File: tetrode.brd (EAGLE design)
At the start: 108 x 101.6 mm, 34 parts, among them IC1 MEGA8-P, J1 AVR_SPI_PROG_3X2NS, U1 LM2576T-5.0/NOPB, Y1 16MHz

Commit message: Started code
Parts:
- removed C5: 22p, resistor:C025-024X044
- removed C6: 470u, resistor:E5-13
- removed C7: 47u, resistor:E2,5-6
- removed D2: (no value), adafruit:DO-1N4148
- removed D3: (no value), adafruit:DO201T15
- removed L1: 100u, resistor:0204/5
- removed P1, P2, P3: (no value), SparkFun-Connectors:1X03
- removed U1: LM2576T-5.0/NOPB, LM2576T:T05A_TEX
- added J2, J3, J4: (no value), SparkFun-Connectors:1X05
- C1: value 47u -> 2.2u; device resistor:E2,5-6 -> resistor:E2-5
- C2: value 470u -> 2.2u; device resistor:E5-13 -> resistor:E2-5
- C4: value 22p -> 2.2u; device resistor:C025-024X044 -> resistor:E2-5
- Y1: value 16MHz -> (none); device SparkFun-Clocks:HC49US -> SparkFun-Clocks:RESONATOR-PTH-7.6X3.8
- moved C4 81.3 mm to (3.81, 49.5)
- moved J1 80.1 mm to (76.2, 5.08)
- moved S2 78.5 mm to (21.6, 69.8)
- moved R5 70.7 mm to (21.6, 61.7)
- moved S3 68.8 mm to (38.1, 69.8)
- moved S4 64.9 mm to (55.9, 69.8)
- moved R6 53.6 mm to (38.1, 61.8)
- moved R4 50.4 mm to (50.8, 47.6)
- moved C2 49.0 mm to (64.8, 50.8)
- moved R8 44.9 mm to (59.7, 50.8), turned to 90 degrees
- moved R2 44.7 mm to (6.35, 62.2), turned to 90 degrees
- moved R7 35.6 mm to (55.9, 61.8)
- moved C1 30.0 mm to (7.62, 69.8)
- moved C3 25.0 mm to (64.8, 57.1)
- moved LS1 16.6 mm to (71.1, 66.0)
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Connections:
- removed net N$5: IC1.25, P3.2
- removed net N$8: D3.C, L1.2, U1.2
- removed net VCC: C1.+, C7.+, D2.C, U1.1
- net +5V: now also CN1.PWR, J2.1, J3.1, J4.1; no longer C2.+, C6.+, L1.1, P1.1, P2.1, P3.1, U1.4
- net GND: now also C4.-, J2.5, J3.5, J4.5, Y1.2; no longer C4.2, C5.2, C6.-, C7.-, D3.A, P1.3, P2.3, P3.3, U1.3, U1.5
- net N$1: now also IC1.23, J2.3; no longer CN1.PWR, D2.A
- net N$3: now also IC1.24, J3.3; no longer IC1.23, P1.2
- net N$4: now also IC1.25, J4.3; no longer IC1.24, P2.2
- net SW1: now also C1.+
- net SW2: now also C2.+
- net SW3: now also C4.+
- net XTAL1: no longer C4.1
- net XTAL2: now also Y1.3; no longer C5.1, Y1.2
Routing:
- net SW3: track 0.00 -> 116.9 mm, vias 0 -> 2
- net RST: track 0.00 -> 107.5 mm
- net RS: track 0.00 -> 96.4 mm, vias 0 -> 1
- net E: track 0.00 -> 93.7 mm, vias 0 -> 1
- net SCK: track 0.00 -> 81.4 mm
- net SW2: track 0.00 -> 81.4 mm
- net VO: track 0.00 -> 81.0 mm, vias 0 -> 1
- net N$4: track 0.00 -> 70.9 mm, vias 0 -> 3
- net XTAL1: track 0.00 -> 64.2 mm, vias 0 -> 2
- net N$3: track 0.00 -> 61.5 mm, vias 0 -> 3
- net N$1: track 0.00 -> 61.4 mm
- net N$7: track 0.00 -> 61.1 mm
- net XTAL2: track 0.00 -> 59.3 mm, vias 0 -> 3
- net SW1: track 0.00 -> 51.4 mm
- net S_FEED: track 0.00 -> 43.7 mm, vias 0 -> 1
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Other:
- board size 108 x 101.6 mm -> 81.3 x 85.1 mm

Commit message: Updates to CAD for board and base, started on code
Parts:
- moved S1 12.7 mm to (29.2, 82.5)
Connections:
- net +5V: now also S1.2; no longer S1.1
- net GND: now also S1.1; no longer S1.2
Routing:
- net S_FEED: track 43.7 -> 56.4 mm
- net SERVO: track 40.0 -> 46.1 mm
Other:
- board text added: "FEEDBACK"
- board text added: "SERVO"
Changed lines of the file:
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@@
 <hole x="49.53" y="5.08" drill="3.401059375"/>
 <hole x="11.43" y="62.23" drill="3.401059375"/>
+<text x="39.37" y="81.28" size="1.778" layer="21">FEEDBACK</text>
+<text x="28.829" y="79.756" size="1.27" layer="21">SERVO</text>
 </plain>
 <attributes>
@@
 <attribute name="VALUE" x="35.9664" y="59.5376" size="0.9906" layer="27" ratio="10"/>
 </element>
-<element name="S1" library="SparkFun-Connectors" library_urn="urn:adsk.eagle:library:513" package="1X04" package3d_urn="urn:adsk.eagle:package:38085/1" value="" x="16.51" y="82.55" smashed="yes">
-<attribute name="NAME" x="15.24" y="83.947" size="0.6096" layer="25" font="vector" ratio="20"/>
-<attribute name="PROD_ID" value="CONN-09696" x="90.17" y="7.62" size="1.778" layer="27" display="off"/>
-<attribute name="VALUE" x="15.24" y="80.518" size="0.6096" layer="27" font="vector" ratio="20"/>
+<element name="S1" library="SparkFun-Connectors" library_urn="urn:adsk.eagle:library:513" package="1X04" package3d_urn="urn:adsk.eagle:package:38085/1" value="" x="29.21" y="82.55" smashed="yes">
+<attribute name="NAME" x="27.94" y="83.947" size="0.6096" layer="25" font="vector" ratio="20"/>
+<attribute name="PROD_ID" value="CONN-09696" x="102.87" y="7.62" size="1.778" layer="27" display="off"/>
+<attribute name="VALUE" x="27.94" y="80.518" size="0.6096" layer="27" font="vector" ratio="20"/>
 </element>
 <element name="VR1" library="SparkFun-Resistors" library_urn="urn:adsk.eagle:library:532" package="TRIMPOT-PTH-3386U" package3d_urn="urn:adsk.eagle:package:39662/1" value="10k" x="74.93" y="52.07" smashed="yes">
@@
 <contactref element="R1" pad="2"/>
 <contactref element="R3" pad="2"/>
-<contactref element="S1" pad="1"/>
 <contactref element="LCD1" pad="2"/>
 <contactref element="R4" pad="2"/>
@@
 <contactref element="J3" pad="1"/>
 <contactref element="J4" pad="1"/>
+<contactref element="S1" pad="2"/>
 </signal>
 <signal name="RST">
@@
 <contactref element="CN1" pad="GNDBREAK"/>
 <contactref element="D1" pad="K"/>
-<contactref element="S1" pad="2"/>
 <contactref element="LCD1" pad="16"/>
 <contactref element="LCD1" pad="1"/>
@@
 <wire x1="18.8" y1="43.44" x2="16.52" y2="45.72" width="0.254" layer="1"/>
 <wire x1="16.52" y1="45.72" x2="11.43" y2="45.72" width="0.254" layer="1"/>
+<contactref element="S1" pad="1"/>
 </signal>
 <signal name="N$2">
@@
 <wire x1="14.27353125" y1="65.87216875" x2="13.2715" y2="66.8742" width="0.254" layer="16"/>
 <wire x1="13.2715" y1="66.8742" x2="13.2715" y2="74.2315" width="0.254" layer="16"/>
-<wire x1="23.3142125" y1="82.55" x2="24.13" y2="82.55" width="0.254" layer="16"/>
-<wire x1="20.3708" y1="81.3308" x2="22.0950125" y2="81.3308" width="0.254" layer="16"/>
-<wire x1="22.0950125" y1="81.3308" x2="23.3142125" y2="82.55" width="0.254" layer="16"/>
+<wire x1="35.6108" y1="81.3308" x2="36.83" y2="82.55" width="0.254" layer="16"/>
+<wire x1="35.6108" y1="81.3308" x2="20.3708" y2="81.3308" width="0.254" layer="16"/>
 <wire x1="13.2715" y1="74.2315" x2="20.3708" y2="81.3308" width="0.254" layer="16"/>
 </signal>
@@
 <wire x1="24.13" y1="66.04" x2="24.13" y2="77.47" width="0.254" layer="16"/>
 <via x="24.13" y="77.47" extent="1-16" drill="0.35"/>
-<wire x1="24.13" y1="77.47" x2="24.13" y2="80.01" width="0.254" layer="1"/>
-<wire x1="24.13" y1="80.01" x2="21.59" y2="82.55" width="0.254" layer="1"/>
+<wire x1="34.29" y1="82.55" x2="29.21" y2="77.47" width="0.254" layer="1"/>
+<wire x1="24.13" y1="77.47" x2="29.21" y2="77.47" width="0.254" layer="1"/>
 </signal>
 <signal name="RS">

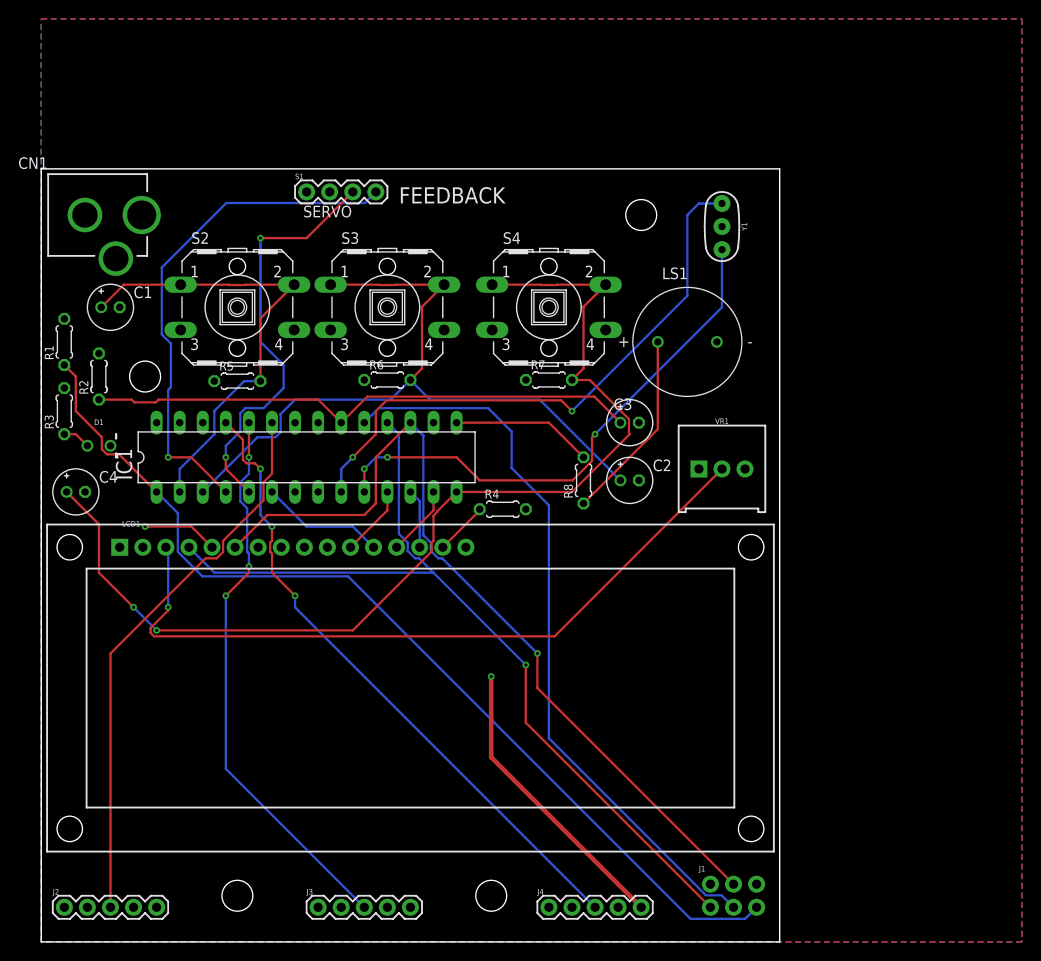
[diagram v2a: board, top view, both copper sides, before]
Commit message: Switched layout of board and reduced max speed of servo to resolve brown out when the servo stops
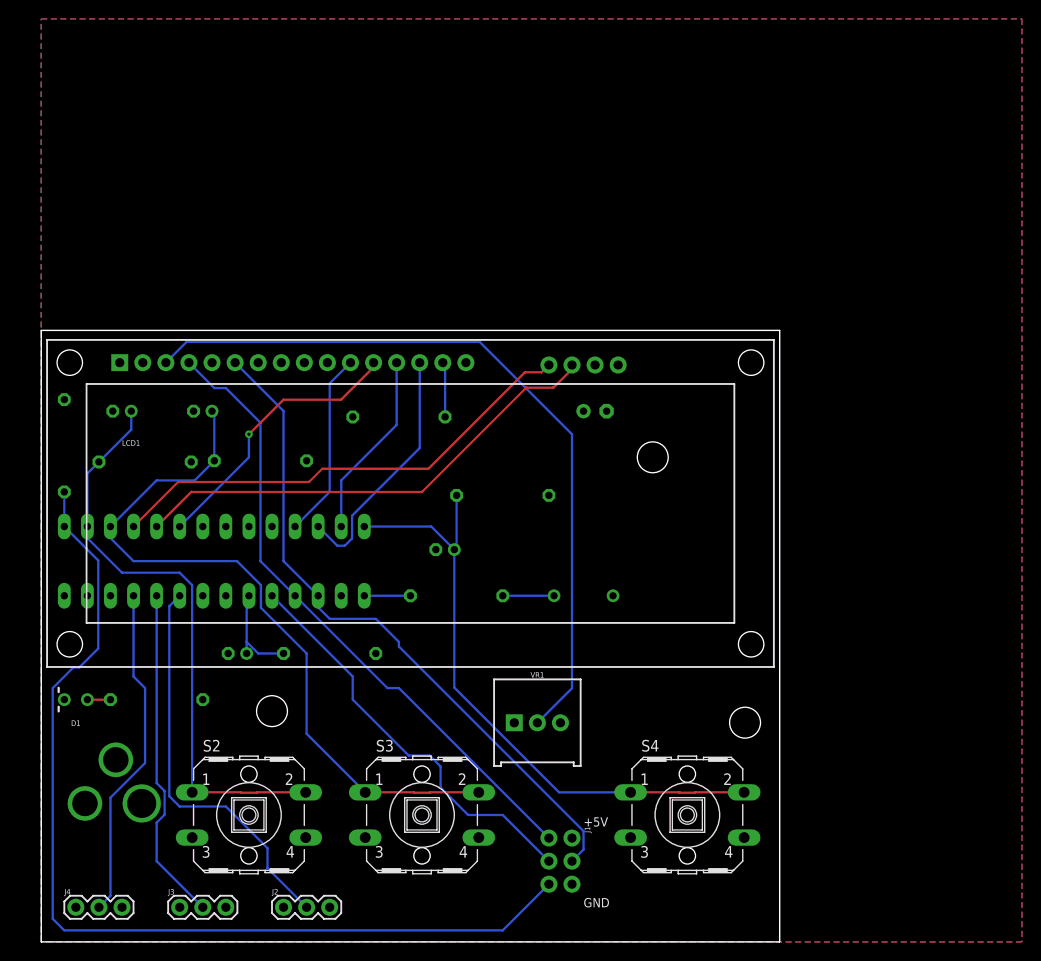
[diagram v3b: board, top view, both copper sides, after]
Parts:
- removed Y1: (no value), SparkFun-Clocks:RESONATOR-PTH-7.6X3.8
- added C5: 47u, resistor:E2,5-6
- J2, J3, J4: device SparkFun-Connectors:1X05 -> SparkFun-Connectors:1X03
- R1, R2, R3, R4, R5, R6, R7, R8: device resistor:0204/5 -> resistor:0309/10
- moved CN1 64.8 mm to (-2.54, 15.2), flipped to the bottom, turned to 90 degrees
- moved S4 57.9 mm to (71.1, 14.0)
- moved S3 56.0 mm to (41.9, 14.0)
- moved S2 55.9 mm to (22.9, 14.0)
- moved J4 52.1 mm to (3.81, 3.81)
- moved C3 50.1 mm to (21.6, 31.8), flipped to the bottom
- moved C2 47.6 mm to (17.8, 58.4), flipped to the bottom
- moved C4 41.1 mm to (44.5, 43.2), flipped to the bottom
- moved R2 39.7 mm to (31.8, 31.8), flipped to the bottom, turned to 180 degrees
- moved S1 39.2 mm to (63.5, 63.5), flipped to the bottom
- moved VR1 34.5 mm to (54.6, 24.1)
- moved R3 33.3 mm to (12.7, 26.7), flipped to the bottom, turned to 180 degrees
- moved LS1 30.2 mm to (59.7, 38.1), flipped to the bottom, turned to 180 degrees
- moved D1 28.1 mm to (3.81, 26.7), turned to 180 degrees
- moved J2 24.1 mm to (26.7, 3.81)
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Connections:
- removed net N$4: IC1.25, J4.3
- removed net XTAL1: IC1.9, Y1.1
- removed net XTAL2: IC1.10, Y1.3
- new net N$5: IC1.25, J4.2
- net +5V: now also C5.+
- net GND: now also C5.-, J2.3, J3.3, J4.3; no longer J2.5, J3.5, J4.5, Y1.2
- net N$1: now also J2.2; no longer J2.3
- net N$3: now also J3.2; no longer J3.3
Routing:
- net N$4: track 70.9 -> 0.00 mm, vias 3 -> 0
- net XTAL1: track 64.2 -> 0.00 mm, vias 2 -> 0
- net XTAL2: track 59.3 -> 0.00 mm, vias 3 -> 0
- net N$7: track 61.1 -> 11.0 mm
- net SW3: track 116.9 -> 68.9 mm, vias 2 -> 0
- net GND: track 40.6 -> 0.00 mm, vias 2 -> 0
- net N$5: track 0.00 -> 36.9 mm
- net SCK: track 81.4 -> 45.4 mm
- net RS: track 96.4 -> 70.2 mm, vias 1 -> 0
- net N$3: track 61.5 -> 37.1 mm, vias 3 -> 0
- net DB7: track 6.51 -> 27.4 mm
- net E: track 93.7 -> 74.3 mm, vias 1 -> 0
- net N$1: track 61.4 -> 44.0 mm
- net DB5: track 13.7 -> 30.6 mm, vias 0 -> 1
- net N$9: track 21.2 -> 5.64 mm
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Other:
- board size 81.3 x 85.1 mm -> 81.3 x 67.3 mm
- board text added: "+5V"
- board text added: "FEED"
- board text added: "GND"
- board text removed: "FEEDBACK"
